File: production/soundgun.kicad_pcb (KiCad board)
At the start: 4 copper layers, 87.5 x 60 mm, 24 parts, among them J1 STX-3000, J3 Screw_Terminal_01x02, J4 Screw_Terminal_01x02, U1 LM358, U2 MIC4427, U3 Pico

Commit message: Cleaned Release project
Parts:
- removed C4, C5: 100n, Capacitor_THT:C_Disc_D3.8mm_W2.6mm_P2.50mm
- removed D2: LED, LED_THT:LED_D5.0mm
- removed H2, H3, H4: MountingHole_Pad, MountingHole:MountingHole_3.2mm_M3_DIN965_Pad
- removed J3, J4: Screw_Terminal_01x02, TerminalBlock_Phoenix:TerminalBlock_Phoenix_PT-1,5-2-3.5-H_1x02_P3.50mm_Horizontal
- removed R6: 10, Resistor_THT:R_Axial_DIN0204_L3.6mm_D1.6mm_P7.62mm_Horizontal
- removed R7: 10k, Resistor_THT:R_Axial_DIN0204_L3.6mm_D1.6mm_P7.62mm_Horizontal
- added J2: Screw_Terminal_01x02, TerminalBlock_Phoenix:TerminalBlock_Phoenix_PT-1,5-2-3.5-H_1x02_P3.50mm_Horizontal, F.Cu at (55.2, 89.2)
- C1: value 10u -> 100n; footprint Capacitor_THT:C_Disc_D4.7mm_W2.5mm_P5.00mm -> Capacitor_THT:C_Disc_D3.8mm_W2.6mm_P2.50mm
- R1: value 22k -> 47k
- R2: value 22k -> 10
- R3: value 47k -> 10k
- R4: value 47k -> 1k
- R5: value 1k -> 22k
- moved U2 90.1 mm to (55.4, 75.5)
- moved R5 73.2 mm to (43.3, 99.3), turned to 0 degrees
- moved U1 63.0 mm to (43.8, 75.5), turned to 0 degrees
- moved R2 60.2 mm to (43.3, 89.8), turned to 0 degrees
- moved R1 59.0 mm to (43.3, 86.7), turned to 0 degrees
- moved R3 53.5 mm to (43.3, 93.0), turned to 0 degrees
- moved C1 50.1 mm to (66.6, 75.5), turned to 0 degrees
- moved R4 46.1 mm to (43.3, 96.2)
- moved H1 44.2 mm to (56.0, 98.3)
- moved D1 44.1 mm to (64.0, 97.0)
- moved C3 38.1 mm to (63.1, 91.2)
- moved C2 30.0 mm to (63.1, 87.2)
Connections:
- C1 pad 1: GND -> unconnected-(C1-Pad1)
- C1 pad 2: /V_OPAMP -> unconnected-(C1-Pad2)
- C2 pad 1: GND -> unconnected-(C2-Pad1)
- C2 pad 2: /VREF -> unconnected-(C2-Pad2)
- C3 pad 1: /AUDIO_IN -> unconnected-(C3-Pad1)
- C3 pad 2: Net-(C3-Pad2) -> unconnected-(C3-Pad2)
- D1 pad 1: GND -> unconnected-(D1-K-Pad1)
- D1 pad 2: /LED_A -> unconnected-(D1-A-Pad2)
- J1 pad 1: GND -> unconnected-(J1-Pad1)
- J1 pad 2: /AUDIO_IN -> unconnected-(J1-Pad2)
- R1 pad 1: Net-(U1A--) -> unconnected-(R1-Pad1)
- R1 pad 2: /ADC_IN -> unconnected-(R1-Pad2)
- R2 pad 1: Net-(C3-Pad2) -> unconnected-(R2-Pad1)
- R2 pad 2: Net-(U1A--) -> unconnected-(R2-Pad2)
- R3 pad 1: /VREF -> unconnected-(R3-Pad1)
- R3 pad 2: +3V3 -> unconnected-(R3-Pad2)
- R4 pad 1: GND -> unconnected-(R4-Pad1)
- R4 pad 2: /VREF -> unconnected-(R4-Pad2)
- R5 pad 1: /LED -> unconnected-(R5-Pad1)
- R5 pad 2: /LED_A -> unconnected-(R5-Pad2)
- U1 pad 1: /ADC_IN -> unconnected-(U1-Pad1)
- U1 pad 2: Net-(U1A--) -> unconnected-(U1A---Pad2)
- U1 pad 3: /VREF -> unconnected-(U1A-+-Pad3)
- U1 pad 8: /V_OPAMP -> unconnected-(U1C-V+-Pad8)
- U2 pad 2: Net-(U2-IN_A) -> unconnected-(U2-IN_A-Pad2)
- U2 pad 3: GND -> unconnected-(U2-GND-Pad3)
- U2 pad 4: Net-(U2-IN_B) -> unconnected-(U2-IN_B-Pad4)
- U2 pad 5: /SPKR_B -> unconnected-(U2-OUT_B-Pad5)
- U2 pad 6: +12V -> unconnected-(U2-V+-Pad6)
- U2 pad 7: /SPKR_A -> unconnected-(U2-OUT_A-Pad7)
- U3 pad 13: GND -> unconnected-(U3-GND-Pad13)
- U3 pad 18: GND -> unconnected-(U3-GND-Pad18)
- U3 pad 19: Net-(U2-IN_B) -> unconnected-(U3-GPIO14-Pad19)
- U3 pad 20: Net-(U2-IN_A) -> unconnected-(U3-GPIO15-Pad20)
- U3 pad 21: /LED -> unconnected-(U3-GPIO16-Pad21)
- U3 pad 23: GND -> unconnected-(U3-GND-Pad23)
- U3 pad 28: GND -> unconnected-(U3-GND-Pad28)
- U3 pad 3: GND -> unconnected-(U3-GND-Pad3)
- U3 pad 31: /ADC_IN -> unconnected-(U3-GPIO26_ADC0-Pad31)
- U3 pad 33: GND -> unconnected-(U3-AGND-Pad33)
- U3 pad 36: +3V3 -> unconnected-(U3-3V3-Pad36)
- U3 pad 38: GND -> unconnected-(U3-GND-Pad38)
- U3 pad 40: +5V -> unconnected-(U3-VBUS-Pad40)
- U3 pad 8: GND -> unconnected-(U3-GND-Pad8)
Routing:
- net Net-(U1A--): track 15.3 -> 0.00 mm
- net /VREF: track 3.77 -> 0.00 mm
- net /ADC_IN: track 3.76 -> 0.00 mm
- added copper zone on In2.Cu, net unconnected-(U3-3V3-Pad36)
- removed copper zone on In2.Cu, net +3V3

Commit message: Added model paths
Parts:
- J1: footprint stx3000:STX-3000_KYC -> Connector_stx3000:STX-3000_KYC
- moved U3 60.4 mm to (187.1, 89.4), turned to 0 degrees
- moved J1 23.8 mm to (67.7, 67.0)

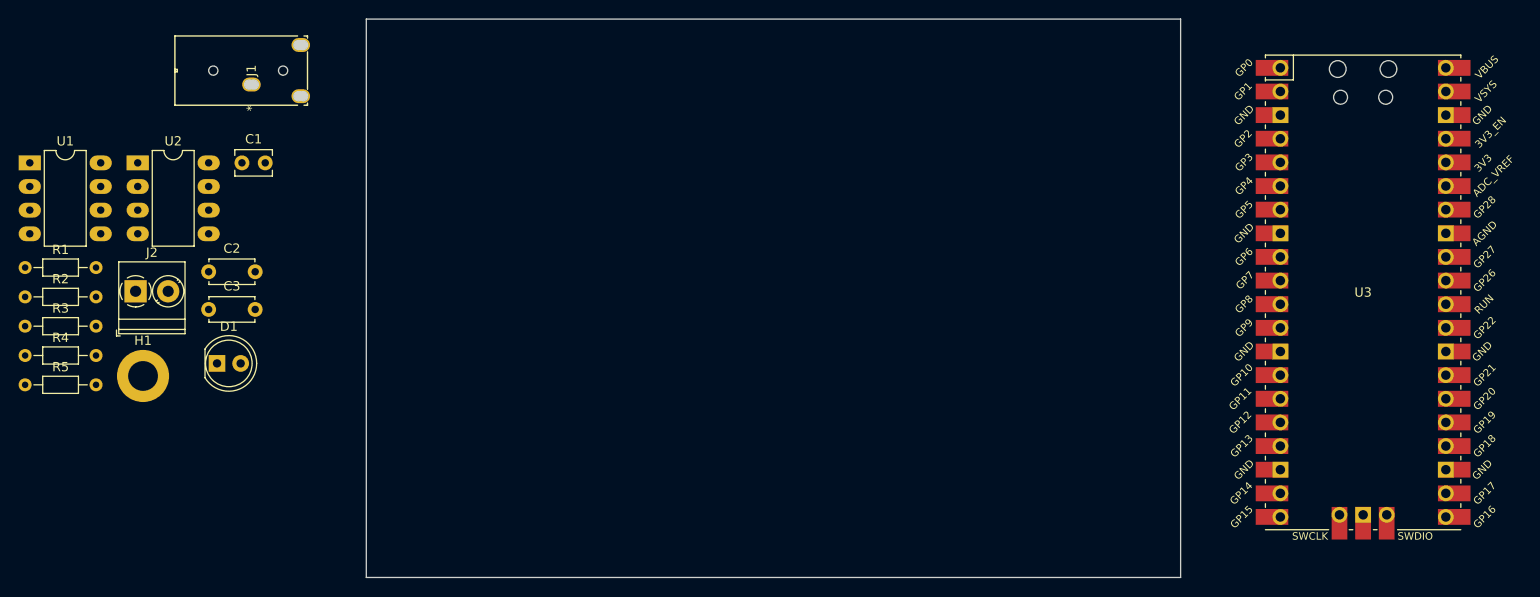
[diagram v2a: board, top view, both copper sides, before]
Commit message: Created production PCB
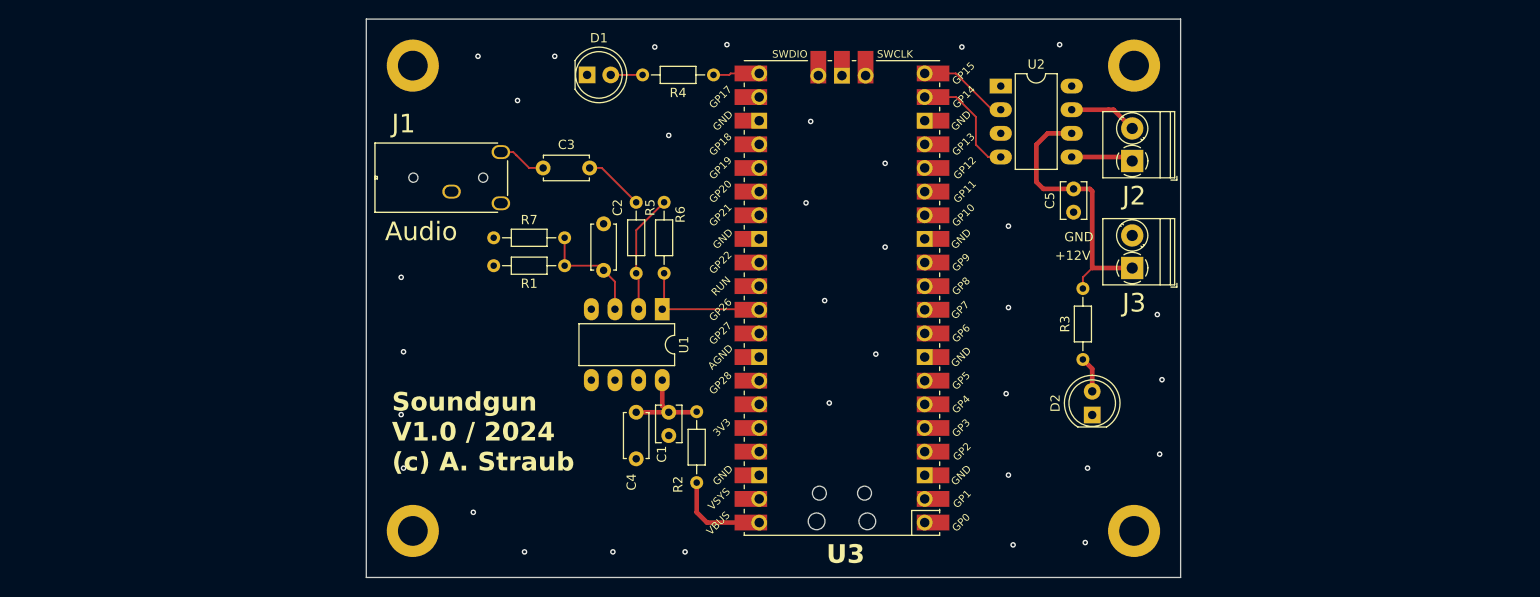
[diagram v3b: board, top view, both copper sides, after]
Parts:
- added C4: 10u, Capacitor_THT:C_Disc_D4.7mm_W2.5mm_P5.00mm, F.Cu at (109.0, 107.2)
- added C5: 100n, Capacitor_THT:C_Disc_D3.8mm_W2.6mm_P2.50mm, F.Cu at (156.0, 80.8)
- added D2: LED, LED_THT:LED_D5.0mm, F.Cu at (158.0, 102.5)
- added H2: MountingHole_Pad, MountingHole:MountingHole_3.2mm_M3_DIN965_Pad, F.Cu at (85.0, 115.0)
- added H3: MountingHole_Pad, MountingHole:MountingHole_3.2mm_M3_DIN965_Pad, F.Cu at (162.5, 115.0)
- added H4: MountingHole_Pad, MountingHole:MountingHole_3.2mm_M3_DIN965_Pad, F.Cu at (162.5, 65.0)
- added J3: Screw_Terminal_01x02, TerminalBlock_Phoenix:TerminalBlock_Phoenix_PT-1,5-2-3.5-H_1x02_P3.50mm_Horizontal, F.Cu at (162.3, 86.8)
- added R6: 22k, Resistor_THT:R_Axial_DIN0204_L3.6mm_D1.6mm_P7.62mm_Horizontal, F.Cu at (112.0, 79.7)
- added R7: 47k, Resistor_THT:R_Axial_DIN0204_L3.6mm_D1.6mm_P7.62mm_Horizontal, F.Cu at (93.7, 83.5)
- moved R3 113.7 mm to (157.0, 96.6), turned to 90 degrees
- moved J2 108.0 mm to (162.3, 75.2), turned to 90 degrees
- moved U2 93.1 mm to (148.2, 67.2)
- moved R4 79.9 mm to (117.3, 66.0), turned to 180 degrees
- moved R2 74.9 mm to (115.5, 109.8), turned to 90 degrees
- moved U1 69.8 mm to (111.8, 91.2), turned to -90 degrees
- moved R5 68.5 mm to (109.0, 79.7), turned to -90 degrees
- moved R1 58.0 mm to (101.3, 86.5), turned to 180 degrees
- moved U3 56.0 mm to (131.1, 90.0), turned to 180 degrees
- moved C1 54.4 mm to (112.5, 104.8), turned to 90 degrees
- moved D1 50.4 mm to (103.7, 66.0)
- moved H1 44.2 mm to (85.0, 65.0)
- moved C2 42.8 mm to (105.5, 82.0), turned to -90 degrees
- moved C3 39.0 mm to (99.0, 76.0)
- moved J1 24.4 mm to (89.2, 78.5)
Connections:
- C1 pad 1: unconnected-(C1-Pad1) -> GND
- C1 pad 2: unconnected-(C1-Pad2) -> /VOPAMP
- C2 pad 1: unconnected-(C2-Pad1) -> GND
- C2 pad 2: unconnected-(C2-Pad2) -> /VREF
- C3 pad 1: unconnected-(C3-Pad1) -> Net-(C3-Pad1)
- C3 pad 2: unconnected-(C3-Pad2) -> Net-(C3-Pad2)
- D1 pad 1: unconnected-(D1-K-Pad1) -> GND
- D1 pad 2: unconnected-(D1-A-Pad2) -> Net-(D1-A)
- J1 pad 1: unconnected-(J1-Pad1) -> GND
- J1 pad 2: unconnected-(J1-Pad2) -> Net-(C3-Pad1)
- J2 pad 1: unconnected-(J2-Pin_1-Pad1) -> /SPKR_B
- J2 pad 2: unconnected-(J2-Pin_2-Pad2) -> /SPKR_A
- R1 pad 1: unconnected-(R1-Pad1) -> /VREF
- R1 pad 2: unconnected-(R1-Pad2) -> +3V3
- R2 pad 1: unconnected-(R2-Pad1) -> +5V
- R2 pad 2: unconnected-(R2-Pad2) -> /VOPAMP
- R3 pad 1: unconnected-(R3-Pad1) -> Net-(D2-A)
- R3 pad 2: unconnected-(R3-Pad2) -> +12V
- R4 pad 1: unconnected-(R4-Pad1) -> Net-(U3-GPIO16)
- R4 pad 2: unconnected-(R4-Pad2) -> Net-(D1-A)
- R5 pad 1: unconnected-(R5-Pad1) -> Net-(C3-Pad2)
- R5 pad 2: unconnected-(R5-Pad2) -> Net-(U1A--)
- U1 pad 1: unconnected-(U1-Pad1) -> /ADC_IN
- U1 pad 2: unconnected-(U1A---Pad2) -> Net-(U1A--)
- U1 pad 3: unconnected-(U1A-+-Pad3) -> /VREF
- U1 pad 8: unconnected-(U1C-V+-Pad8) -> /VOPAMP
- U2 pad 2: unconnected-(U2-IN_A-Pad2) -> Net-(U2-IN_A)
- U2 pad 3: unconnected-(U2-GND-Pad3) -> GND
- U2 pad 4: unconnected-(U2-IN_B-Pad4) -> Net-(U2-IN_B)
- U2 pad 5: unconnected-(U2-OUT_B-Pad5) -> /SPKR_B
- U2 pad 6: unconnected-(U2-V+-Pad6) -> +12V
- U2 pad 7: unconnected-(U2-OUT_A-Pad7) -> /SPKR_A
- U3 pad 13: unconnected-(U3-GND-Pad13) -> GND
- U3 pad 18: unconnected-(U3-GND-Pad18) -> GND
- U3 pad 19: unconnected-(U3-GPIO14-Pad19) -> Net-(U2-IN_B)
- U3 pad 20: unconnected-(U3-GPIO15-Pad20) -> Net-(U2-IN_A)
- U3 pad 21: unconnected-(U3-GPIO16-Pad21) -> Net-(U3-GPIO16)
- U3 pad 23: unconnected-(U3-GND-Pad23) -> GND
- U3 pad 28: unconnected-(U3-GND-Pad28) -> GND
- U3 pad 3: unconnected-(U3-GND-Pad3) -> GND
- U3 pad 31: unconnected-(U3-GPIO26_ADC0-Pad31) -> /ADC_IN
- U3 pad 33: unconnected-(U3-AGND-Pad33) -> GND
- U3 pad 37: unconnected-(U3-3V3_EN-Pad37) -> +3V3
- U3 pad 38: unconnected-(U3-GND-Pad38) -> GND
- U3 pad 40: unconnected-(U3-VBUS-Pad40) -> +5V
- U3 pad 8: unconnected-(U3-GND-Pad8) -> GND
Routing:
- net +12V: track 0.00 -> 30.4 mm
- net /ADC_IN: track 0.00 -> 14.4 mm
- net Net-(U1A--): track 0.00 -> 12.8 mm
- net Net-(U2-IN_B): track 0.00 -> 12.6 mm
- net /VREF: track 0.00 -> 12.1 mm
- net +5V: track 0.00 -> 10.4 mm
- net /VOPAMP: track 0.00 -> 10.3 mm
- net Net-(U2-IN_A): track 0.00 -> 9.79 mm
- net /SPKR_A: track 0.00 -> 7.34 mm
- net /SPKR_B: track 0.00 -> 6.68 mm
- net Net-(C3-Pad2): track 0.00 -> 6.53 mm
- net Net-(C3-Pad1): track 0.00 -> 5.25 mm
- net Net-(U3-GPIO16): track 0.00 -> 4.98 mm
- net Net-(D2-A): track 0.00 -> 3.84 mm
- net Net-(D1-A): track 0.00 -> 3.42 mm
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- added copper zone on In2.Cu, net +3V3
- removed copper zone on In2.Cu, net unconnected-(U3-3V3-Pad36)_0
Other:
- board text added: "+12V"
- board text added: "Audio"
- board text added: "GND"
- board text added: "Soundgun V1.0 / 2024 (c) A. Straub"
